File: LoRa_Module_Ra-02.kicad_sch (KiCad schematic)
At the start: 2 parts, among them U301 Ra-02

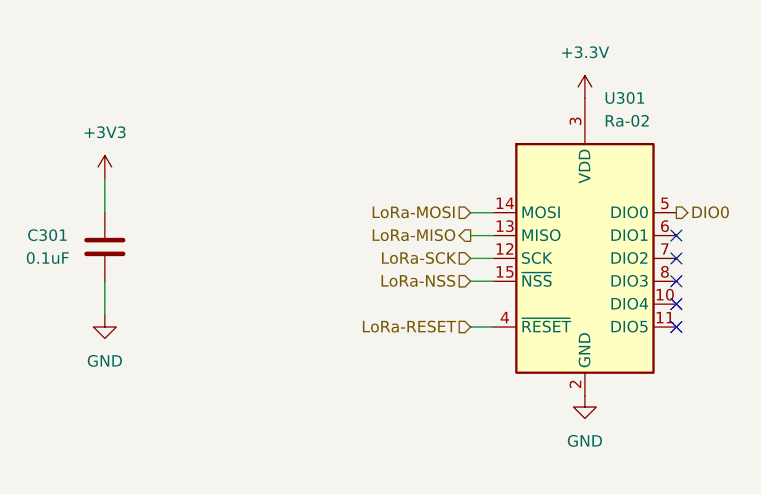
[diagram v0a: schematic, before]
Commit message: "3.3V buck boost converter added. few footprints added"
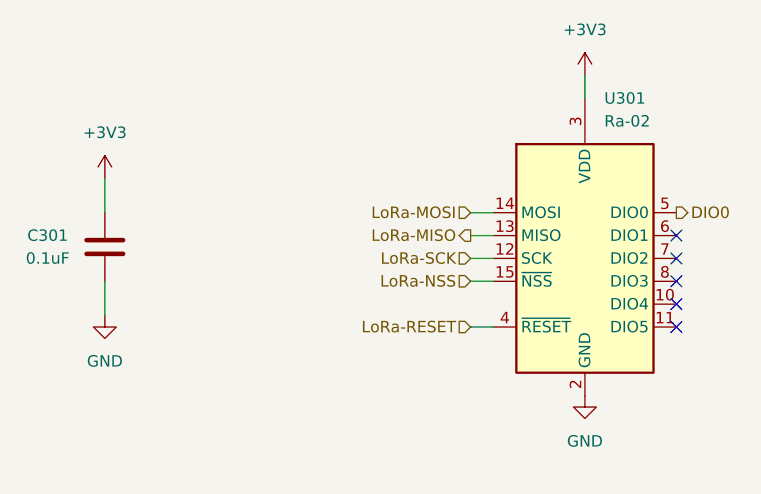
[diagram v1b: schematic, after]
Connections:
- net +3.3V is gone; now on net +3V3: U301.3 (VDD)
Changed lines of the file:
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@@
+	(wire
+		(pts
+			(xy 161.29 76.2) (xy 161.29 78.74)
+		)
+		(stroke
+			(width 0)
+			(type default)
+		)
+	)
 	(wire
 		(pts
@@
 	)
 	(symbol
-		(lib_id "power:+3.3V")
-		(at 161.29 78.74 0)
-		(unit 1)
-		(exclude_from_sim no)
-		(in_bom yes)
-		(on_board yes)
-		(dnp no)
-		(fields_autoplaced yes)
-		(property "Reference" "#PWR0301"
-			(at 161.29 82.55 0)
-			(effects
-				(font
-					(size 1.27 1.27)
-				)
-				(hide yes)
-			)
-		)
-		(property "Value" "+3.3V"
-			(at 161.29 73.66 0)
-			(effects
-				(font
-					(size 1.27 1.27)
-				)
-			)
-		)
-		(property "Footprint" ""
-			(at 161.29 78.74 0)
-			(effects
-				(font
-					(size 1.27 1.27)
-				)
-				(hide yes)
-			)
-		)
-		(property "Datasheet" ""
-			(at 161.29 78.74 0)
-			(effects
-				(font
-					(size 1.27 1.27)
-				)
-				(hide yes)
-			)
-		)
-		(property "Description" "Power symbol creates a global label with name \"+3.3V\""
-			(at 161.29 78.74 0)
-			(effects
-				(font
-					(size 1.27 1.27)
-				)
-				(hide yes)
-			)
-		)
-		(pin "1"
-		)
-		(instances
-			(project ""
-				(path "/ba95ddf4-72c6-4eeb-9c09-ae7c8e5af670/541b98c8-c699-4d8e-bb05-fa473644b143"
-					(reference "#PWR0301")
-					(unit 1)
-				)
-			)
-		)
-	)
-	(symbol
 		(lib_id "power:GND")
 		(at 161.29 111.76 0)
@@
 					(unit 1)
 				)
+			)
+		)
+	)
+	(symbol
+		(lib_id "power:+3V3")
+		(at 161.29 76.2 0)
+		(unit 1)
+		(exclude_from_sim no)
+		(in_bom yes)
+		(on_board yes)
+		(dnp no)
+		(fields_autoplaced yes)
+		(property "Reference" "#PWR0301"
+			(at 161.29 80.01 0)
+			(effects
+				(font
+					(size 1.27 1.27)
+				)
+				(hide yes)
+			)
+		)
+		(property "Value" "+3V3"
+			(at 161.29 71.12 0)
+			(effects
+				(font
+					(size 1.27 1.27)
+				)
+			)
+		)
+		(property "Footprint" ""
+			(at 161.29 76.2 0)
+			(effects
+				(font
+					(size 1.27 1.27)
+				)
+				(hide yes)
+			)
+		)
+		(property "Datasheet" ""
+			(at 161.29 76.2 0)
+			(effects
+				(font
+					(size 1.27 1.27)
+				)
+				(hide yes)
+			)
+		)
+		(property "Description" "Power symbol creates a global label with name \"+3V3\""
+			(at 161.29 76.2 0)
+			(effects
+				(font
+					(size 1.27 1.27)
+				)
+				(hide yes)
+			)
+		)
+		(pin "1"
+		)
+		(instances
+			(project ""
+				(path "/ba95ddf4-72c6-4eeb-9c09-ae7c8e5af670/541b98c8-c699-4d8e-bb05-fa473644b143"
+					(reference "#PWR0301")
+					(unit 1)
+				)

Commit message: "Assign Footprints Done"
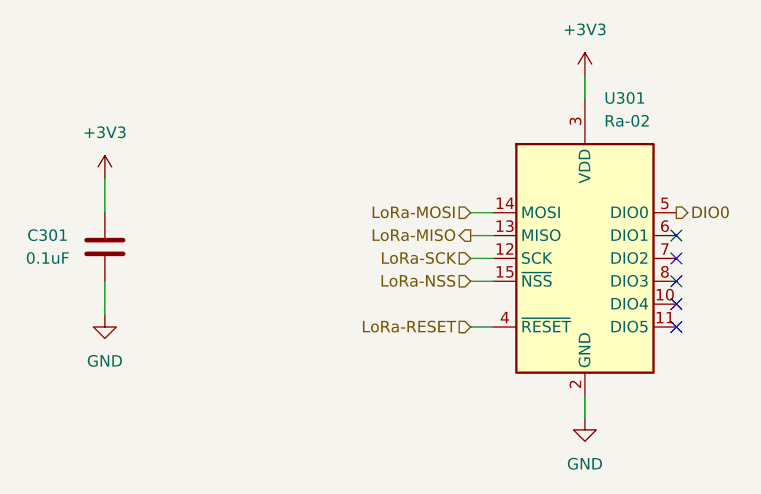
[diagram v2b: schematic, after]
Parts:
- C301: footprint (none) -> Capacitor_SMD:C_0402_1005Metric_Pad0.74x0.62mm_HandSolder
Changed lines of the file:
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@@
+	(wire
+		(pts
+			(xy 161.29 114.3) (xy 161.29 111.76)
+		)
+		(stroke
+			(width 0)
+			(type default)
+		)
+	)
 	(wire
 		(pts
@@
 			)
 		)
-		(property "Footprint" ""
+		(property "Footprint" "Capacitor_SMD:C_0402_1005Metric_Pad0.74x0.62mm_HandSolder"
 			(at 106.9848 99.06 0)
 			(effects
@@
 		(dnp no)
 		(fields_autoplaced yes)
-		(property "Reference" "#PWR0303"
+		(property "Reference" "#PWR0302"
 			(at 107.95 109.22 0)
 			(effects
@@
 			(project "govi_v3_trh_sensor_kicad"
 				(path "/ba95ddf4-72c6-4eeb-9c09-ae7c8e5af670/541b98c8-c699-4d8e-bb05-fa473644b143"
-					(reference "#PWR0303")
+					(reference "#PWR0302")
 					(unit 1)
 				)
@@
 	(symbol
 		(lib_id "power:GND")
-		(at 161.29 111.76 0)
+		(at 161.29 114.3 0)
 		(unit 1)
 		(exclude_from_sim no)
@@
 		(dnp no)
 		(fields_autoplaced yes)
-		(property "Reference" "#PWR0302"
-			(at 161.29 118.11 0)
+		(property "Reference" "#PWR0304"
+			(at 161.29 120.65 0)
 			(effects
 				(font
@@
 		)
 		(property "Value" "GND"
-			(at 161.29 116.84 0)
+			(at 161.29 119.38 0)
 			(effects
 				(font
@@
 		)
 		(property "Footprint" ""
-			(at 161.29 111.76 0)
+			(at 161.29 114.3 0)
 			(effects
 				(font
@@
 		)
 		(property "Datasheet" ""
-			(at 161.29 111.76 0)
+			(at 161.29 114.3 0)
 			(effects
 				(font
@@
 		)
 		(property "Description" "Power symbol creates a global label with name \"GND\" , ground"
-			(at 161.29 111.76 0)
+			(at 161.29 114.3 0)
 			(effects
 				(font
@@
 			(project ""
 				(path "/ba95ddf4-72c6-4eeb-9c09-ae7c8e5af670/541b98c8-c699-4d8e-bb05-fa473644b143"
-					(reference "#PWR0302")
+					(reference "#PWR0304")
 					(unit 1)
 				)
@@
 		(dnp no)
 		(fields_autoplaced yes)
-		(property "Reference" "#PWR0304"
+		(property "Reference" "#PWR0301"
 			(at 107.95 91.44 0)
 			(effects
@@
 			(project ""
 				(path "/ba95ddf4-72c6-4eeb-9c09-ae7c8e5af670/541b98c8-c699-4d8e-bb05-fa473644b143"
-					(reference "#PWR0304")
+					(reference "#PWR0301")
 					(unit 1)
 				)
@@
 		(dnp no)
 		(fields_autoplaced yes)
-		(property "Reference" "#PWR0301"
+		(property "Reference" "#PWR0303"
 			(at 161.29 80.01 0)
 			(effects
@@
 			(project ""
 				(path "/ba95ddf4-72c6-4eeb-9c09-ae7c8e5af670/541b98c8-c699-4d8e-bb05-fa473644b143"
-					(reference "#PWR0301")
+					(reference "#PWR0303")
 					(unit 1)
 				)
